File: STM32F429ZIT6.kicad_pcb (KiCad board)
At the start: 4 copper layers, 86.6 x 72.7 mm, 115 parts, among them J1 Conn_02x24_Odd_Even, J2 Conn_01x05_Pin, J3 Conn_02x24_Odd_Even, SW1 K3-1235S, U2 LD3985M33R, U3 MCP6004, U4 NAU88C22YG_C914209, U5 RCLAMP0521P.TCT_C3029033, U6 RCLAMP0521P.TCT_C3029033, U7 W9825G6KH-6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

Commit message: quick save
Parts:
- J1, J3: value Conn_02x24_Odd_Even -> Conn_02x30_Odd_Even; footprint Connector_PinHeader_2.54mm:PinHeader_2x24_P2.54mm_Vertical -> Connector_PinHeader_2.54mm:PinHeader_2x30_P2.54mm_Vertical
- moved J3 15.2 mm to (196.8, 44.7)
- moved J1 14.4 mm to (118.6, 44.7)
- moved D2 6.73 mm to (138.9, 112.5)
- moved R4 6.73 mm to (140.2, 113.8)
- moved R5 6.73 mm to (143.9, 114.2)
- moved USBC1 6.73 mm to (141.5, 118.2)
- moved R29 5.26 mm to (156.8, 81.1), turned to 90 degrees
- moved D4 2.21 mm to (154.5, 80.8), turned to -90 degrees
- moved C42 1.12 mm to (176.4, 63.2)
- moved C43 1.12 mm to (176.4, 65.7)
- moved C44 1.12 mm to (176.4, 68.2)
- moved R27 0.84 mm to (155.9, 81.1), turned to -90 degrees
- moved LED1 0.43 mm to (158.4, 80.6), turned to -90 degrees
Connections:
- J1 pad 10: /PB9 -> /PG10
- J1 pad 12: /PE2 -> /PG11
- J1 pad 14: /PE3 -> /PG12
- J1 pad 16: /PE4 -> /PB4
- J1 pad 18: /PE5 -> /PB7
- J1 pad 2: /PG12 -> unconnected-(J1-Pin_2-Pad2)
- J1 pad 20: /PE6 -> /PB8
- J1 pad 22: /PC13 -> /PB9
- J1 pad 24: /PC14 -> /PE2
- J1 pad 26: /PC15 -> /PE3
- J1 pad 28: /PF6 -> /PE4
- J1 pad 30: /PF7 -> /PE5
- J1 pad 32: /PF8 -> /PE6
- J1 pad 34: /PF9 -> /PC13
- J1 pad 36: /PF10 -> /PC14
- J1 pad 38: /PC1 -> /PC15
- J1 pad 4: /PB4 -> /PD6
- J1 pad 40: /PC2 -> /PF6
- J1 pad 42: /PC3 -> /PF7
- J1 pad 44: /PA0 -> /PF8
- J1 pad 46: /PA1 -> /PF9
- J1 pad 48: /PA2 -> /PF10
- J1 pad 6: /PB7 -> /PD7
- J1 pad 8: /PB8 -> /PG9
- J3 pad 1: /PD2 -> unconnected-(J3-Pin_1-Pad1)
- J3 pad 11: /PC8 -> /PA12
- J3 pad 13: /PG7 -> /PA11
- J3 pad 15: /PG6 -> /PA10
- J3 pad 17: /PD13 -> /PA9
- J3 pad 19: /PD12 -> /PC8
- J3 pad 21: /PB13 -> /PC6
- J3 pad 23: /PB12 -> /PG7
- J3 pad 25: /PB11 -> /PG6
- J3 pad 27: /PB10 -> /PD13
- J3 pad 29: /PB2 -> /PD12
- J3 pad 3: /PA12 -> /PD5
- J3 pad 31: /PB1 -> /PD11
- J3 pad 33: /PB0 -> /PB13
- J3 pad 35: /PC5 -> /PB12
- J3 pad 37: /PC4 -> /PB11
- J3 pad 39: /PA7 -> /PB10
- J3 pad 41: /PA6 -> /PB2
- J3 pad 43: /PA5 -> /PB1
- J3 pad 45: /PA4 -> /PB0
- J3 pad 47: /PA3 -> /PC5
- J3 pad 5: /PA11 -> /PD4
- J3 pad 7: /PA10 -> /PD3
- J3 pad 9: /PA9 -> /PD2
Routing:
- net /PA11: track 0.00 -> 53.2 mm, vias 0 -> 2
- net /PG6: track 0.00 -> 50.4 mm, vias 0 -> 1
- net /PA12: track 0.04 -> 50.4 mm, vias 0 -> 2
- net /PG7: track 0.00 -> 49.8 mm, vias 0 -> 1
- net /PA9: track 0.00 -> 48.1 mm, vias 0 -> 3
- net /PD12: track 0.00 -> 48.1 mm, vias 0 -> 2
- net /PB13: track 0.00 -> 47.9 mm, vias 0 -> 2
- net /PA10: track 0.00 -> 47.4 mm, vias 0 -> 2
- net /PB12: track 0.00 -> 45.6 mm, vias 0 -> 2
- net /PC6: track 0.00 -> 43.8 mm, vias 0 -> 2
- net /PC8: track 0.00 -> 43.7 mm, vias 0 -> 2
- net /PD13: track 0.00 -> 43.0 mm, vias 0 -> 2
- net /PD11: track 0.00 -> 41.8 mm, vias 0 -> 2
- net +5V: track 7.71 -> 4.83 mm
- net /PB14: track 32.6 -> 30.2 mm, vias 2 -> 0
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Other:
- board size 86.6 x 72.7 mm -> 86.6 x 80.8 mm

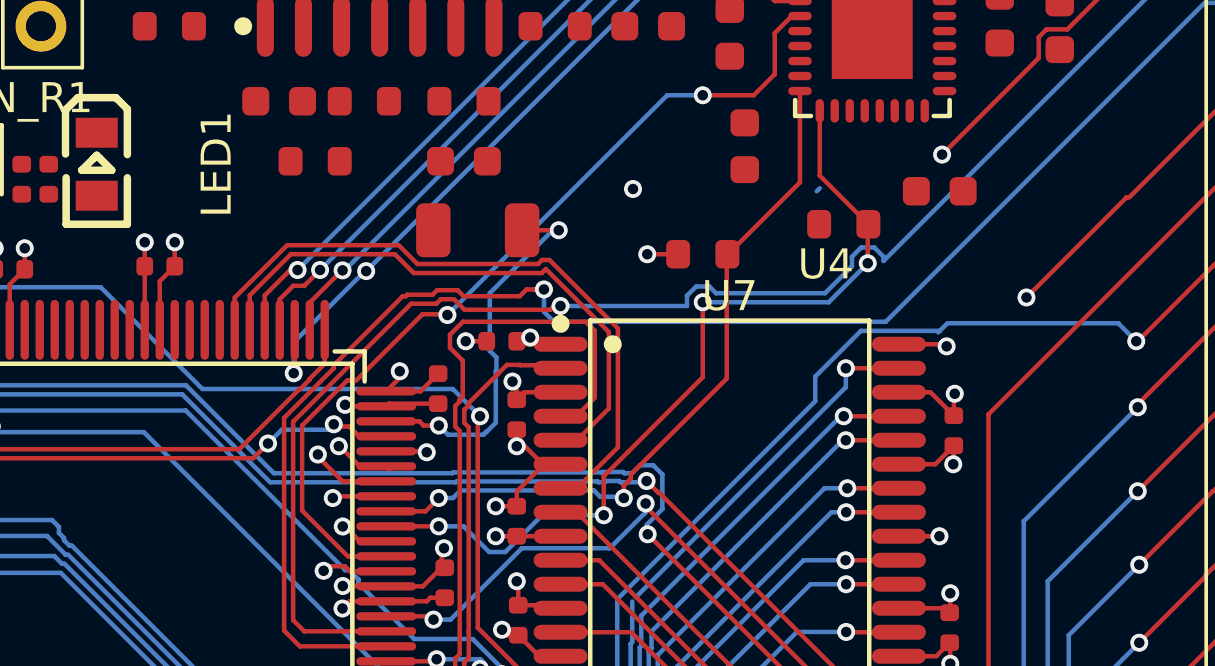
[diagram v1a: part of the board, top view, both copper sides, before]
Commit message: removing the traces i did on inner layers, gotta keep them clean. moving sd ram to the left to make room
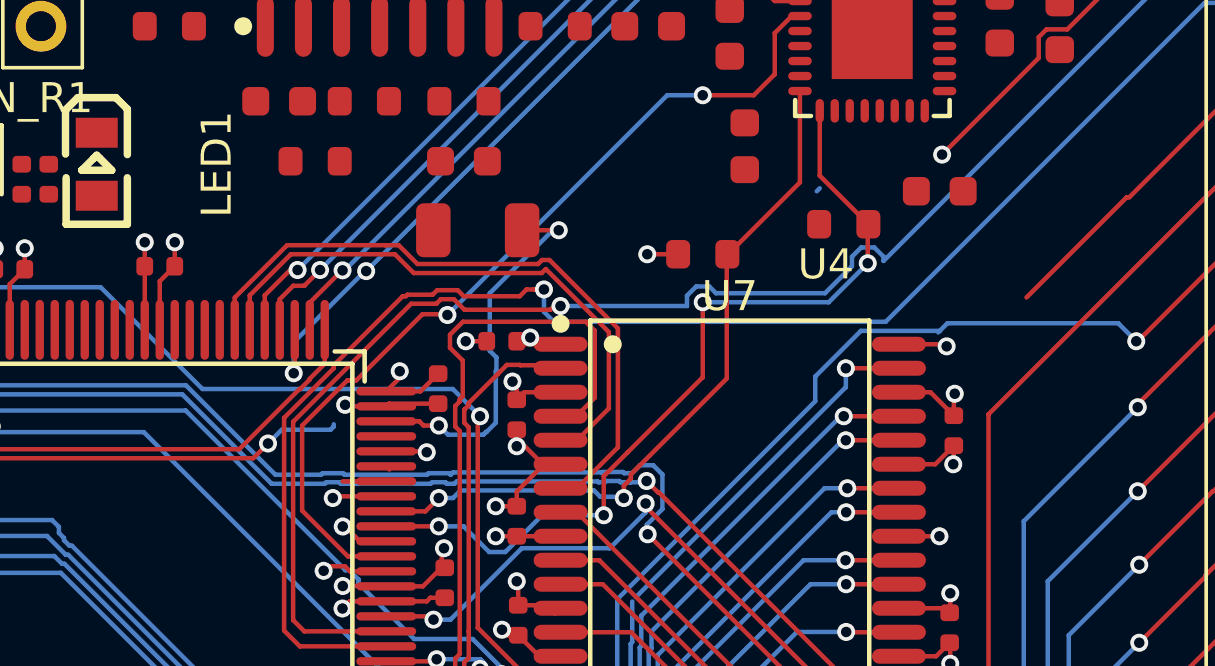
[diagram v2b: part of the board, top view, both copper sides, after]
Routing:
- net /PA12: track 50.4 -> 8.13 mm
- net /PA11: track 53.2 -> 17.1 mm, vias 2 -> 1
- net /PC8: track 43.7 -> 8.98 mm
- net /PA9: track 48.1 -> 16.0 mm, vias 3 -> 2
- net /PA10: track 47.4 -> 16.5 mm, vias 2 -> 1
- net /PD13: track 43.0 -> 13.2 mm, vias 2 -> 1
- net /PC6: track 43.8 -> 18.7 mm
- net /PD12: track 48.1 -> 26.3 mm
- net /SWDIO: track 38.6 -> 37.6 mm, vias 2 -> 1

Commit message: save before i break everything out instead idk why i didnt do that
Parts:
- moved C33 83.4 mm to (160.3, -4.76)
- moved C34 83.4 mm to (150.6, -18.7)
- moved C35 83.4 mm to (146.0, -7.26)
- moved C36 83.4 mm to (167.1, -15.3)
- moved C37 83.4 mm to (160.5, -15.3)
- moved C38 83.4 mm to (166.5, -2.76)
- moved C39 83.4 mm to (180.1, -11.8)
- moved C40 83.4 mm to (172.6, -7.26)
- moved C41 83.4 mm to (169.3, -10.3)
- moved C42 83.4 mm to (172.2, -20.1)
- moved C43 83.4 mm to (172.2, -17.6)
- moved C44 83.4 mm to (172.2, -15.1)
- moved C45 83.4 mm to (178.3, -27.3)
- moved C46 83.4 mm to (178.3, -24.8)
- moved C47 83.4 mm to (178.3, -22.3)
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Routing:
- net /PG6: track 50.4 -> 14.6 mm, vias 1 -> 0
- net /PD13: track 13.2 -> 39.8 mm
- net /PB2: track 58.8 -> 33.6 mm
- net /I2S_BCLK: track 30.5 -> 5.89 mm, vias 3 -> 2
- net /I2S_DOUT: track 26.5 -> 3.47 mm, vias 2 -> 1
- net /I2S_LRKCLK: track 24.1 -> 2.52 mm, vias 2 -> 1
- net /PB1: track 57.2 -> 35.9 mm
- net /I2S_DIN: track 24.2 -> 2.97 mm, vias 2 -> 1
- net /PC5: track 55.8 -> 36.0 mm
- net /D1: track 23.8 -> 4.62 mm
- net /PB0: track 56.3 -> 38.6 mm
- net /PC4: track 55.4 -> 38.9 mm
- net /PC8: track 8.98 -> 24.2 mm, vias 2 -> 0
- net /PG7: track 49.8 -> 34.8 mm, vias 1 -> 0
- net /PA7: track 55.9 -> 42.5 mm
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- added copper zone on In1.Cu, net +3.3V
- added copper zone on In2.Cu, net GND
- removed copper zone on In2.Cu, net +3.3V
- removed copper zone on In1.Cu, net GND

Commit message: KILL ME!!!!!!!!!!!
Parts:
- removed J1, J3: Conn_02x30_Odd_Even, Connector_PinHeader_2.54mm:PinHeader_2x30_P2.54mm_Vertical
- added P1: Header 32X2, Connector_PinHeader_2.54mm:PinHeader_2x32_P2.54mm_Vertical, B.Cu at (118.4, 45.8)
- added P2: Header 32X2, Connector_PinHeader_2.54mm:PinHeader_2x32_P2.54mm_Vertical, B.Cu at (122.0, 126.0)
- added SB26: Circuit Breaker, Jumper:SolderJumper-2_P1.3mm_Open_TrianglePad1.0x1.5mm, F.Cu at (187.9, 113.5)
- added SB27: Circuit Breaker, Jumper:SolderJumper-2_P1.3mm_Open_TrianglePad1.0x1.5mm, F.Cu at (189.0, 117.4)
- moved USBC1 72.7 mm to (207.9, 88.6), turned to 90 degrees
- moved R4 67.7 mm to (203.5, 89.9), turned to 0 degrees
- moved D2 66.8 mm to (202.2, 91.2), turned to 0 degrees
- moved R5 66.2 mm to (203.9, 86.2), turned to -90 degrees
- moved R21 12.0 mm to (158.4, -18.3)
- moved R22 12.0 mm to (158.4, -16.1)
- moved C45 12.0 mm to (179.0, -15.3)
- moved C46 12.0 mm to (179.0, -12.8)
- moved C47 12.0 mm to (179.0, -10.3)
- moved HP_OUT1 12.0 mm to (166.6, -13.8)
- moved L2 12.0 mm to (187.1, 1.47)
- moved R15 12.0 mm to (164.7, -5.33)
- moved R16 12.0 mm to (167.9, -5.33)
- moved R19 12.0 mm to (173.5, -15.3)
- moved R20 12.0 mm to (173.5, -11.3)
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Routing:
- net /PD11: track 41.8 -> 96.3 mm, vias 2 -> 1
- net /PA3: track 56.8 -> 4.14 mm
- net /PA6: track 55.6 -> 4.93 mm
- net /PA5: track 55.2 -> 5.00 mm
- net /PA4: track 54.9 -> 4.92 mm
- net /D13: track 26.1 -> 75.0 mm
- net /D14: track 26.8 -> 74.6 mm
- net /PB13: track 47.9 -> 3.58 mm, vias 2 -> 1
- net /PD13: track 39.8 -> 0.90 mm, vias 1 -> 0
- net /BA1: track 10.3 -> 48.5 mm, vias 2 -> 4
- net /PB12: track 45.6 -> 7.68 mm, vias 2 -> 1
- net /PA7: track 42.5 -> 4.72 mm
- net /PC4: track 38.9 -> 3.23 mm
- net /PB0: track 38.6 -> 3.38 mm
- net /BA0: track 9.12 -> 44.2 mm, vias 2 -> 4
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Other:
- board size 86.6 x 80.8 mm -> 95.7 x 95.7 mm
